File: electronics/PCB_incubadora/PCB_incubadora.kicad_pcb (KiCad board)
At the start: 2 copper layers, 109 x 77 mm, 14 parts, among them J1 HDR-4x1, J10 HDR-2x1, J11 HDR-2x1, J2 HDR-4x1, J3 HDR-2x1, J4 HDR-4x1, J5 HDR-5x1, J6 Conn_02x04_Odd_Even, J7 HDR-4x1, J8 Conn_02x04_Odd_Even, J9 HDR-2x1, X1 ESP32-DevKit, X2 EasyDriver, X3 DC-DC

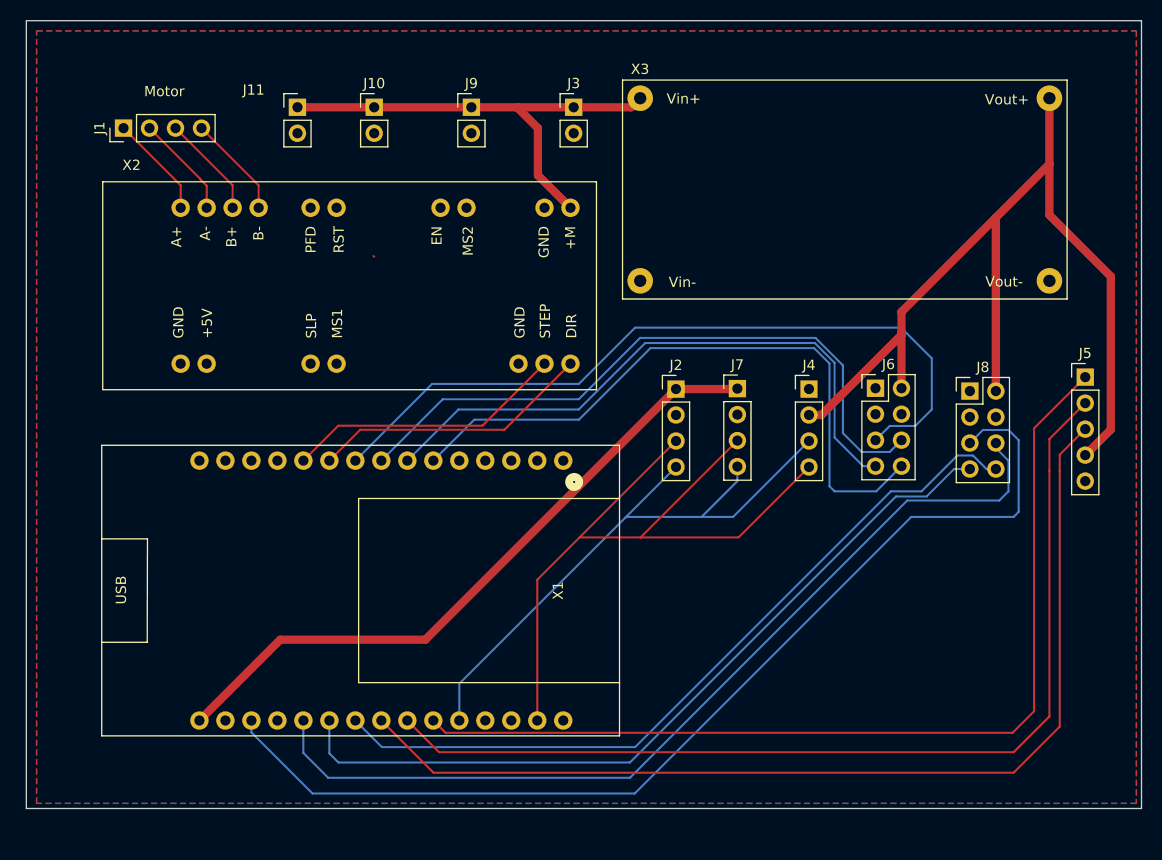
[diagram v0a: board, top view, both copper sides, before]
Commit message: updating 3d model of pcb
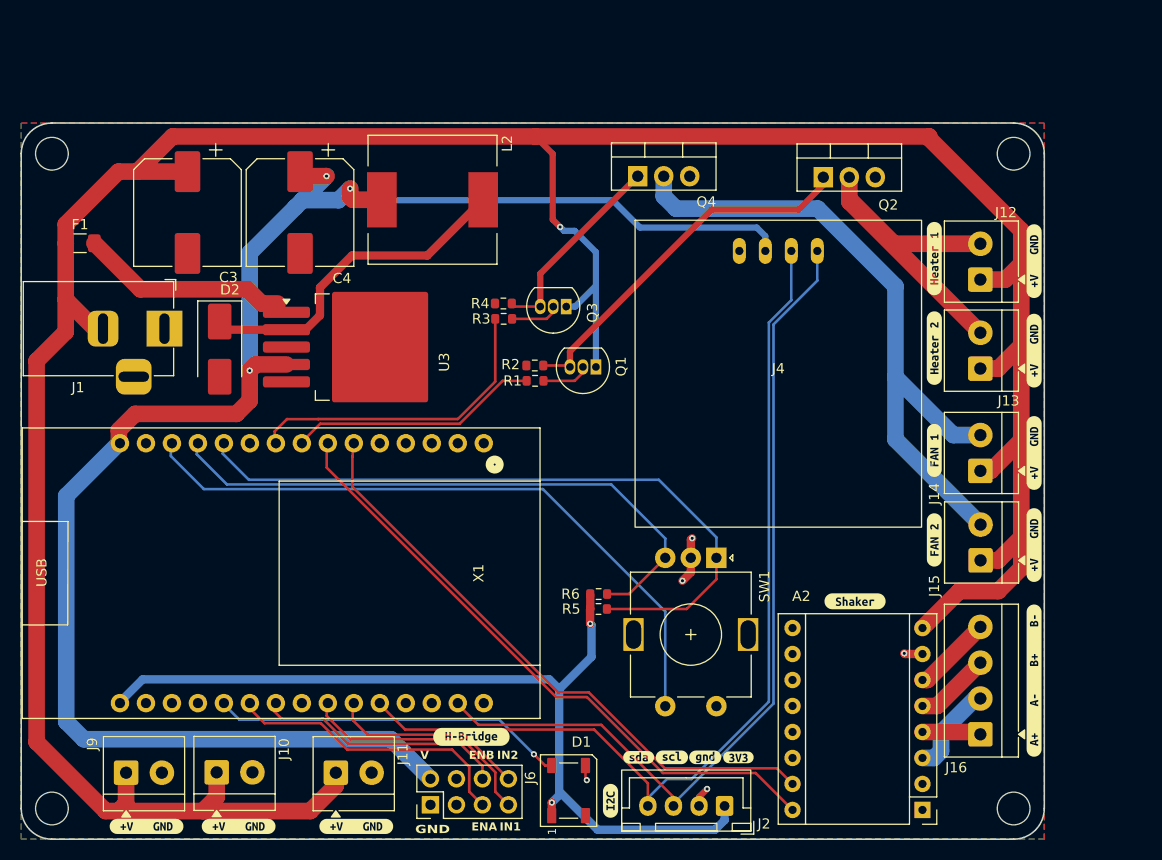
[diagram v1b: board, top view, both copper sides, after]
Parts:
- removed J3: HDR-2x1, Connector_PinHeader_2.54mm:PinHeader_1x02_P2.54mm_Vertical
- removed J5: HDR-5x1, Connector_PinHeader_2.54mm:PinHeader_1x05_P2.54mm_Vertical
- removed J7: HDR-4x1, Connector_PinHeader_2.54mm:PinHeader_1x04_P2.54mm_Vertical
- removed J8: Conn_02x04_Odd_Even, Connector_PinHeader_2.54mm:PinHeader_2x04_P2.54mm_Vertical
- removed X2: EasyDriver, IoWLabsModules:EasyDriver
- removed X3: DC-DC, IoWLabsModules:LM2596
- added A2: Pololu_Breakout_DRV8825, Module:Pololu_Breakout-16_15.2x20.3mm, F.Cu at (128.1, 107.1)
- added C3: 680uF, Capacitor_SMD:CP_Elec_10x10, F.Cu at (56.2, 48.8)
- added C4: 330uF, Capacitor_SMD:CP_Elec_10x10, F.Cu at (67.2, 48.8)
- added D1: WS2812B, LED_SMD:LED_WS2812B_PLCC4_5.0x5.0mm_P3.2mm, F.Cu at (93.5, 105.2)
- added D2: D_Schottky, Diode_SMD:D_SMB_Handsoldering, F.Cu at (59.4, 62.1)
- added F1: FUSE, Fuse:Fuse_1206_3216Metric, F.Cu at (45.8, 51.8)
- added J12: Conn_01x02, TerminalBlock_4Ucon:TerminalBlock_4Ucon_1x02_P3.50mm_Horizontal, F.Cu at (133.8, 55.3)
- added J13: Conn_01x02, TerminalBlock_4Ucon:TerminalBlock_4Ucon_1x02_P3.50mm_Horizontal, F.Cu at (133.8, 64.0)
- added J14: Conn_01x02, TerminalBlock_4Ucon:TerminalBlock_4Ucon_1x02_P3.50mm_Horizontal, F.Cu at (133.8, 74.0)
- added J15: Conn_01x02, TerminalBlock_4Ucon:TerminalBlock_4Ucon_1x02_P3.50mm_Horizontal, F.Cu at (133.8, 82.8)
- added J16: Conn_01x04, TerminalBlock_4Ucon:TerminalBlock_4Ucon_1x04_P3.50mm_Horizontal, F.Cu at (133.8, 99.8)
- added L2: 68uH, Inductor_SMD:L_12x12mm_H6mm, F.Cu at (80.2, 47.5)
- added Q1: BC558, Package_TO_SOT_THT:TO-92_Inline, F.Cu at (96.2, 63.8)
- added Q2: IRF540N, Package_TO_SOT_THT:TO-220-3_Vertical, F.Cu at (118.4, 45.3)
- added Q3: BC558, Package_TO_SOT_THT:TO-92_Inline, F.Cu at (93.3, 57.9)
- added Q4: IRF540N, Package_TO_SOT_THT:TO-220-3_Vertical, F.Cu at (100.3, 45.2)
- added R1: 1k, Resistor_SMD:R_0603_1608Metric, F.Cu at (90.2, 65.2)
- added R2: 10k, Resistor_SMD:R_0603_1608Metric, F.Cu at (90.2, 63.7)
- added R3: 1k, Resistor_SMD:R_0603_1608Metric, F.Cu at (87.2, 59.1)
- added R4: 10k, Resistor_SMD:R_0603_1608Metric, F.Cu at (87.1, 57.6)
- added R5: 10k, Resistor_SMD:R_0603_1608Metric, F.Cu at (96.4, 87.5)
- added R6: 10k, Resistor_SMD:R_0603_1608Metric, F.Cu at (96.4, 86.0)
- added REF**: MountingHole_3.2mm_M3, MountingHole:MountingHole_3.2mm_M3, F.Cu at (43.0, 107.0)
- added REF**: MountingHole_3.2mm_M3, MountingHole:MountingHole_3.2mm_M3, F.Cu at (43.0, 43.0)
- added REF**: MountingHole_3.2mm_M3, MountingHole:MountingHole_3.2mm_M3, F.Cu at (137.0, 43.0)
- added REF**: MountingHole_3.2mm_M3, MountingHole:MountingHole_3.2mm_M3, F.Cu at (137.0, 107.0)
- added SW1: RotaryEncoder_Switch, Rotary_Encoder:RotaryEncoder_Alps_EC11E-Switch_Vertical_H20mm, F.Cu at (108.0, 82.5)
- added U3: LM2596S-5, Package_TO_SOT_SMD:TO-263-5_TabPin3, F.Cu at (73.6, 61.9)
- added kibuzzard-6A5B10A0: G***, kibuzzard-6A5B10A0, F.Cu at (129.2, 53.2)
- added kibuzzard-6A5B10F5: G***, kibuzzard-6A5B10F5, F.Cu at (72.8, 108.8)
- added kibuzzard-6A5B10F5: G***, kibuzzard-6A5B10F5, F.Cu at (61.2, 108.8)
- added kibuzzard-6A5B10F5: G***, kibuzzard-6A5B10F5, F.Cu at (139.0, 62.2)
- added kibuzzard-6A5B10F5: G***, kibuzzard-6A5B10F5, F.Cu at (52.2, 108.8)
- added kibuzzard-6A5B10F5: G***, kibuzzard-6A5B10F5, F.Cu at (139.0, 81.2)
- added kibuzzard-6A5B10F5: G***, kibuzzard-6A5B10F5, F.Cu at (139.0, 53.5)
- added kibuzzard-6A5B10F5: G***, kibuzzard-6A5B10F5, F.Cu at (139.0, 72.2)
- added kibuzzard-6A5B1115: G***, kibuzzard-6A5B1115, F.Cu at (129.2, 62.0)
- added kibuzzard-6A5B1189: G***, kibuzzard-6A5B1189, F.Cu at (129.2, 72.0)
- added kibuzzard-6A5B11C6: G***, kibuzzard-6A5B11C6, F.Cu at (129.2, 80.8)
- added kibuzzard-6A5B1258: G***, kibuzzard-6A5B1258, F.Cu at (139.0, 94.5)
- added kibuzzard-6A5B1282: G***, kibuzzard-6A5B1282, F.Cu at (121.5, 86.8)
- added kibuzzard-6A5B1312: G***, kibuzzard-6A5B1312, F.Cu at (97.6, 106.2)
- added kibuzzard-6A5B13D0: G***, kibuzzard-6A5B13D0, F.Cu at (100.3, 102.0)
- added kibuzzard-6A5B13E5: G***, kibuzzard-6A5B13E5, F.Cu at (103.6, 102.0)
- added kibuzzard-6A5B13F6: G***, kibuzzard-6A5B13F6, F.Cu at (106.8, 102.0)
- added kibuzzard-6A5B1426: G***, kibuzzard-6A5B1426, F.Cu at (110.1, 102.0)
- added kibuzzard-6A5B162D: G***, kibuzzard-6A5B162D, F.Cu at (84.0, 100.0)
- J1: value HDR-4x1 -> Barrel_Jack; footprint Connector_PinHeader_2.54mm:PinHeader_1x04_P2.54mm_Vertical -> Connector_BarrelJack:BarrelJack_Horizontal
- J10, J11, J9: footprint Connector_PinHeader_2.54mm:PinHeader_1x02_P2.54mm_Vertical -> TerminalBlock_4Ucon:TerminalBlock_4Ucon_1x02_P3.50mm_Horizontal
- J2: footprint Connector_PinHeader_2.54mm:PinHeader_1x04_P2.54mm_Vertical -> Connector_JST:JST_XH_B4B-XH-A_1x04_P2.50mm_Vertical
- J4: footprint Connector_PinHeader_2.54mm:PinHeader_1x04_P2.54mm_Vertical -> IoWLabsModules:OLED 0'96 SPI module
- moved J9 73.3 mm to (50.2, 103.5)
- moved J10 66.8 mm to (59.1, 103.5)
- moved J11 65.1 mm to (70.8, 103.5)
- moved J6 59.6 mm to (80.0, 106.6), turned to 90 degrees
- moved J2 41.0 mm to (108.8, 106.8), turned to 180 degrees
- moved J1 20.0 mm to (54.0, 60.1), turned to 0 degrees
- moved X1 7.95 mm to (85.2, 84.0)
- moved J4 3.35 mm to (114.0, 64.5)
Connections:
- net 5V renamed +5V
- J1 pad 1: A+ -> GND
- J1 pad 2: A- -> +12V
- J1 pad 3: B+ -> (no net)
- J10 pad 1: 12V -> +12V
- J11 pad 1: 12V -> +12V
- J9 pad 1: 12V -> +12V
- X1 pad 10: DIR -> unconnected-(X1-27-Pad10)
- X1 pad 11: STEP -> RE_CLK
- X1 pad 12: unconnected-(X1-Pad12) -> RE_DT
- X1 pad 13: unconnected-(X1-Pad13) -> RE_SW
- X1 pad 18: ENA_CH2 -> unconnected-(X1-D15-Pad18)
- X1 pad 20: ENB_CH2 -> RGB
- X1 pad 21: IN1_CH2 -> ENA_CH1
- X1 pad 22: IN2_CH2 -> ENB_CH1
- X1 pad 23: SW -> unconnected-(X1-D5-Pad23)
- X1 pad 24: DT -> IN1_CH1
- X1 pad 25: CLK -> IN2_CH1
- X1 pad 4: CH_H -> unconnected-(X1-34-Pad4)
- X1 pad 5: CH_C -> unconnected-(X1-35-Pad5)
- X1 pad 6: IN2_CH1 -> STEP
- X1 pad 7: IN1_CH1 -> DIR
- X1 pad 8: ENB_CH1 -> HEATER_PWM
- X1 pad 9: ENA_CH1 -> FAN_PWM
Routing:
- net +12V: track 0.00 -> 299.3 mm, vias 0 -> 1
- net ENA_CH2: track 102.8 -> 0.00 mm
- net SW: track 100.4 -> 0.00 mm
- net DT: track 97.6 -> 0.00 mm
- net CLK: track 94.8 -> 0.00 mm
- net ENB_CH2: track 89.9 -> 0.00 mm
- net IN1_CH2: track 78.1 -> 0.00 mm
- net IN2_CH2: track 76.0 -> 0.00 mm
- net +5V: track 95.8 -> 171.5 mm, vias 0 -> 3
- net RE_CLK: track 0.00 -> 68.7 mm
- net FAN-: track 0.00 -> 65.6 mm
- net RE_SW: track 0.00 -> 65.1 mm
- net RE_DT: track 0.00 -> 59.3 mm
- net ENA_CH1: track 74.7 -> 28.6 mm
- net 12V: track 45.9 -> 0.00 mm
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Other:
- board size 109 x 77 mm -> 100 x 70 mm
- board text added: "ENA"
- board text added: "ENB"
- board text added: "GND"
- board text added: "IN1"
- board text added: "IN2"
- board text added: "V"
- board text removed: "Motor"
